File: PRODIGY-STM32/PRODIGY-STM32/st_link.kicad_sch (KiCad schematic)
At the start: 27 parts, among them Q1 BC850, U1 STM32F103C8Tx, Y1 8MHz

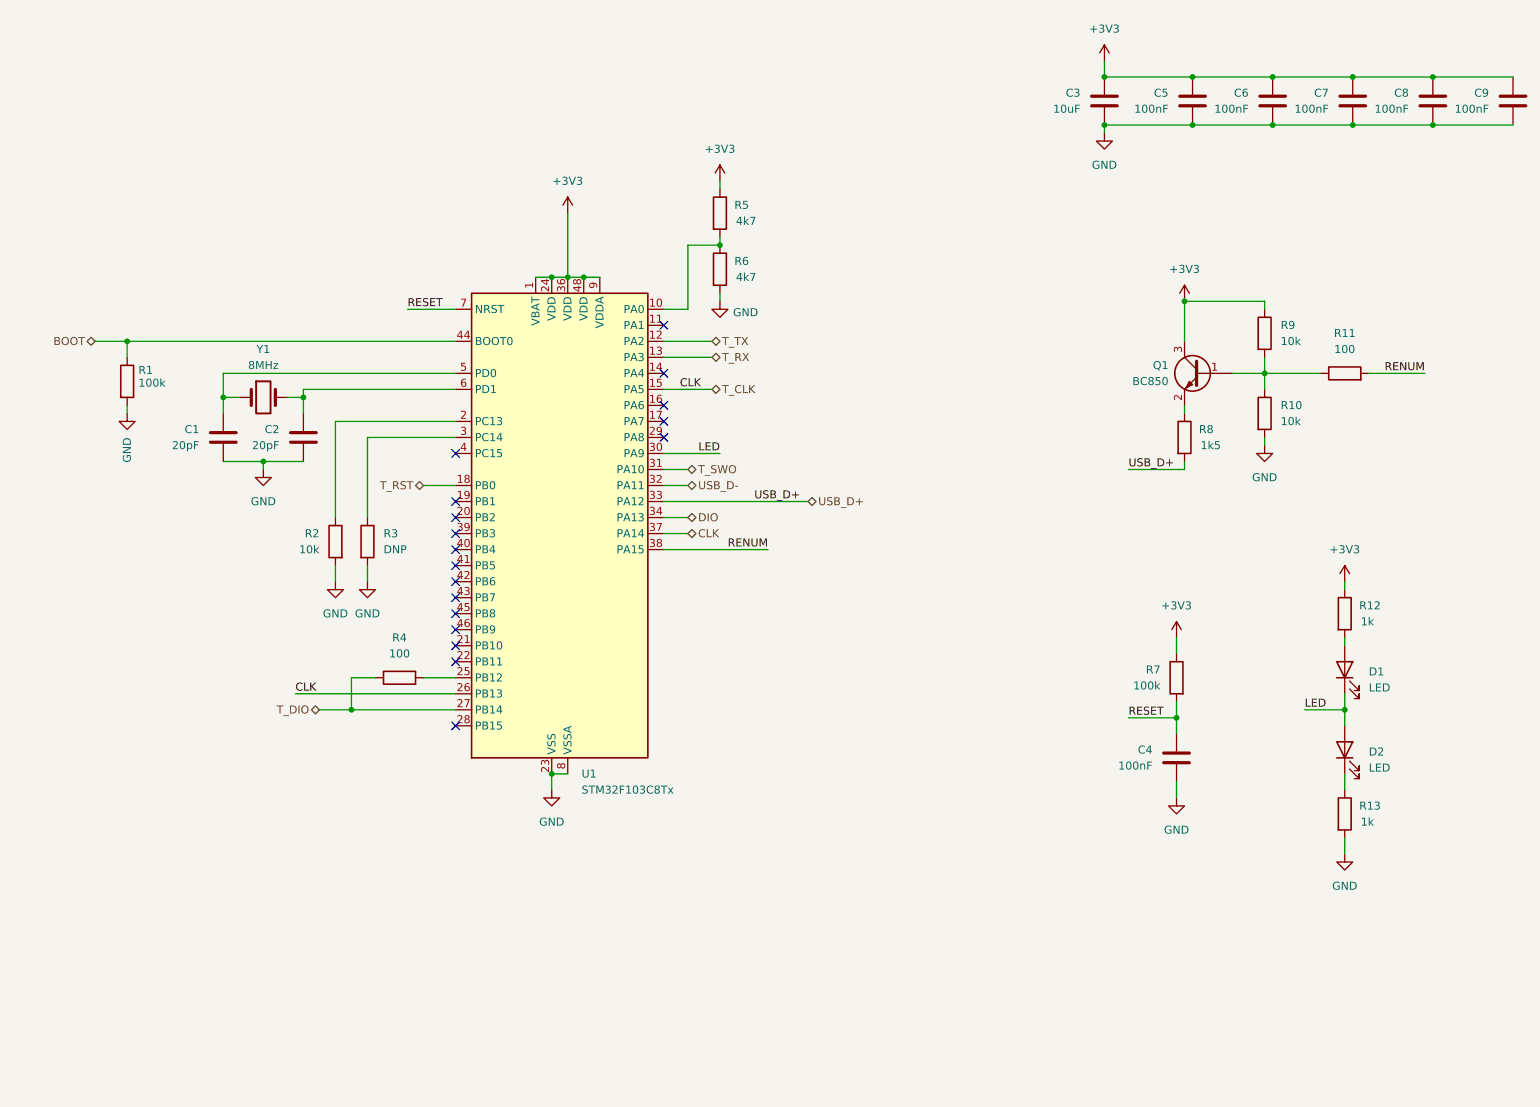
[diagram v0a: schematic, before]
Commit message: stm32 schematic finished
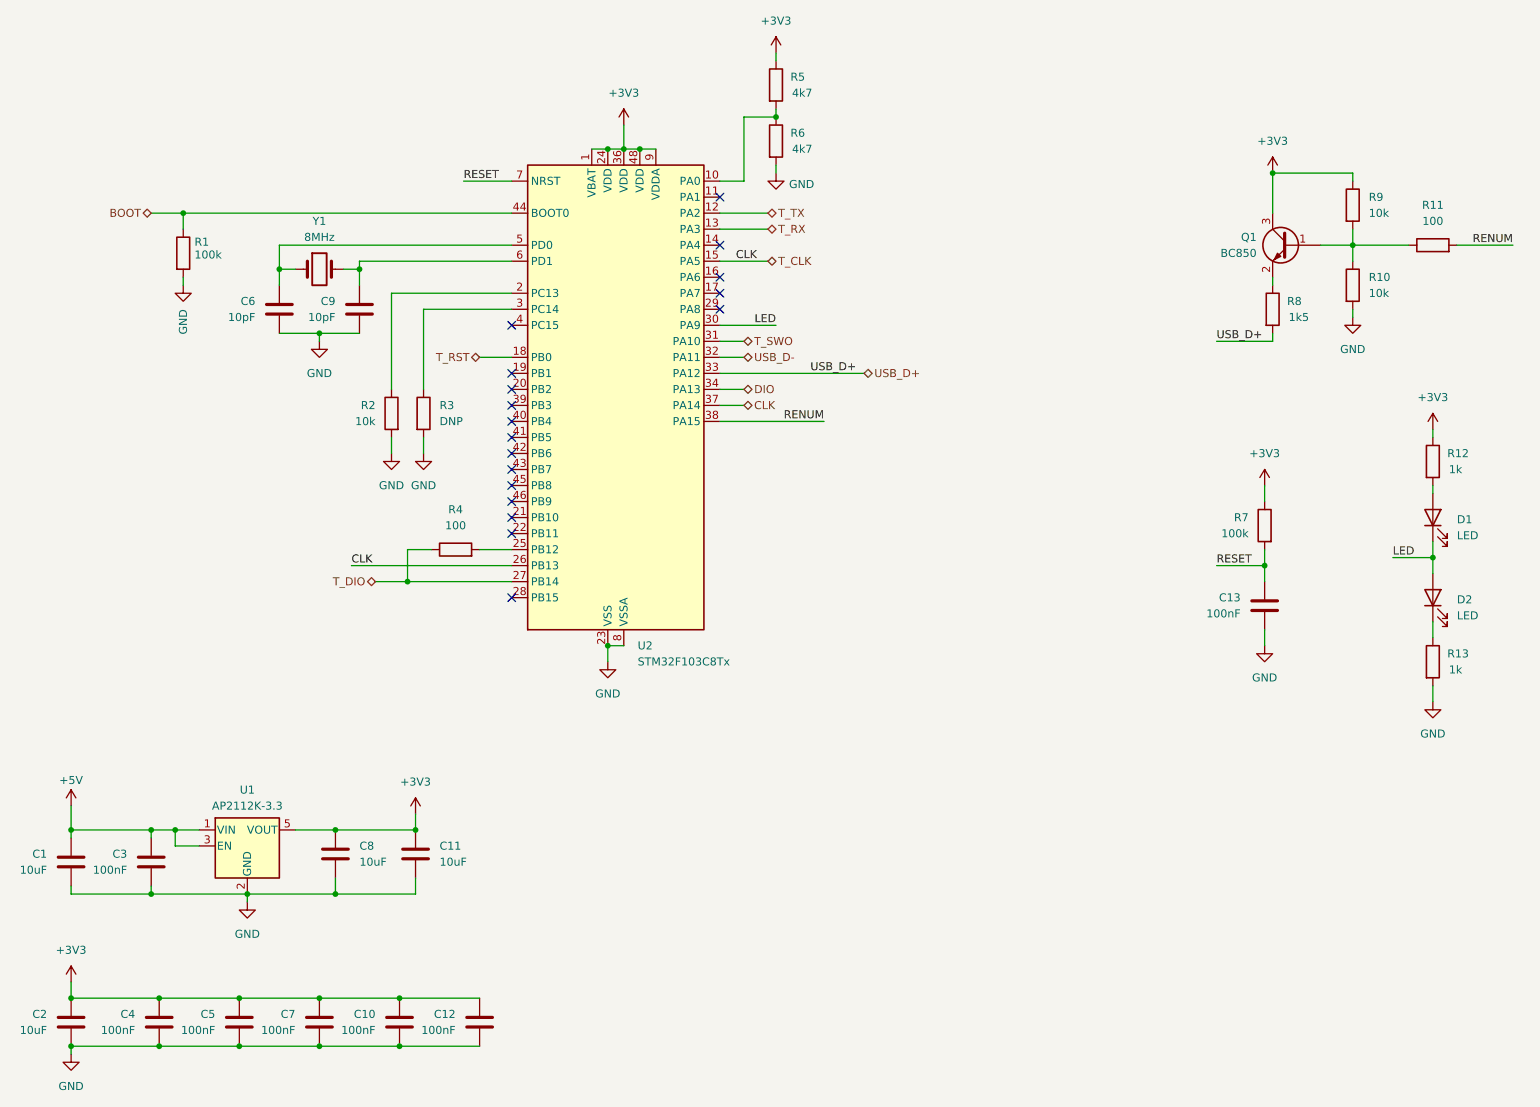
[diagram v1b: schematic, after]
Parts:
- added C1, C11, C8: 10uF, symbol Device:C
- added C3: 100nF, symbol Device:C
- added U1: AP2112K-3.3, Package_TO_SOT_SMD:SOT-23-5, symbol Regulator_Linear:AP2112K-3.3
- C6: renamed from C1; value 20pF -> 10pF
- C9: renamed from C2; value 20pF -> 10pF
- renumbered C8 to C10, C9 to C12, C4 to C13, C3 to C2, C5 to C4, C6 to C5, U1 to U2
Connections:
- net +3V3: now also C11.1, C8.1, U1.5 (VOUT)
- net GND: now also C1.2, C11.2, C3.2, C8.2, U1.2 (GND)
- new net +5V: C1.1, C3.1, U1.1 (VIN), U1.3 (EN)
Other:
- moved on the sheet: C10, C12, C13, C2, C4, C5, C6, C7, C9, D1, D2, Q1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

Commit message: All footprint assosiations have been made across all schematics.
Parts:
- C1, C11, C2, C8: footprint (none) -> Capacitor_SMD:C_0805_2012Metric
- C10, C12, C13, C3, C4, C5, C6, C7, C9: footprint (none) -> Capacitor_SMD:C_0603_1608Metric
- D1, D2: footprint (none) -> LED_SMD:LED_0805_2012Metric
- R1, R10, R11, R12, R13, R2, R3, R4, R5, R6, R7, R8, R9: footprint (none) -> Resistor_SMD:R_0603_1608Metric
- Y1: footprint (none) -> Crystal:Crystal_SMD_3225-4Pin_3.2x2.5mm
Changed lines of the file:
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@@
 			)
 		)
-		(property "Footprint" ""
+		(property "Footprint" "Capacitor_SMD:C_0603_1608Metric"
 			(at 222.5548 119.38 0)
 			(effects
@@
 			)
 		)
-		(property "Footprint" ""
+		(property "Footprint" "Resistor_SMD:R_0603_1608Metric"
 			(at 86.868 85.09 90)
 			(effects
@@
 			)
 		)
-		(property "Footprint" ""
+		(property "Footprint" "Resistor_SMD:R_0603_1608Metric"
 			(at 144.272 33.02 90)
 			(effects
@@
 			)
 		)
-		(property "Footprint" ""
+		(property "Footprint" "Capacitor_SMD:C_0603_1608Metric"
 			(at 98.0948 185.42 0)
 			(effects
@@
 			)
 		)
-		(property "Footprint" ""
+		(property "Footprint" "Capacitor_SMD:C_0603_1608Metric"
 			(at 85.3948 185.42 0)
 			(effects
@@
 			)
 		)
-		(property "Footprint" ""
+		(property "Footprint" "Capacitor_SMD:C_0805_2012Metric"
 			(at 33.3248 160.02 0)
 			(effects
@@
 			)
 		)
-		(property "Footprint" ""
+		(property "Footprint" "Capacitor_SMD:C_0603_1608Metric"
 			(at 59.9948 185.42 0)
 			(effects
@@
 			)
 		)
-		(property "Footprint" ""
+		(property "Footprint" "Resistor_SMD:R_0603_1608Metric"
 			(at 50.292 59.69 90)
 			(effects
@@
 			)
 		)
-		(property "Footprint" ""
+		(property "Footprint" "Capacitor_SMD:C_0603_1608Metric"
 			(at 72.6948 185.42 0)
 			(effects
@@
 			)
 		)
-		(property "Footprint" ""
+		(property "Footprint" "Resistor_SMD:R_0603_1608Metric"
 			(at 235.712 52.07 90)
 			(effects
@@
 			)
 		)
-		(property "Footprint" ""
+		(property "Footprint" "Capacitor_SMD:C_0603_1608Metric"
 			(at 79.0448 72.39 0)
 			(effects
@@
 			)
 		)
-		(property "Footprint" ""
+		(property "Footprint" "Capacitor_SMD:C_0603_1608Metric"
 			(at 47.2948 185.42 0)
 			(effects
@@
 			)
 		)
-		(property "Footprint" ""
+		(property "Footprint" "Resistor_SMD:R_0603_1608Metric"
 			(at 88.392 85.09 90)
 			(effects
@@
 			)
 		)
-		(property "Footprint" ""
+		(property "Footprint" "Capacitor_SMD:C_0603_1608Metric"
 			(at 66.3448 72.39 0)
 			(effects
@@
 			)
 		)
-		(property "Footprint" ""
+		(property "Footprint" "Resistor_SMD:R_0603_1608Metric"
 			(at 95.25 108.458 90)
 			(effects
@@
 			)
 		)
-		(property "Footprint" ""
+		(property "Footprint" "Resistor_SMD:R_0603_1608Metric"
 			(at 248.412 124.46 90)
 			(effects
@@
 			)
 		)
-		(property "Footprint" ""
+		(property "Footprint" "LED_SMD:LED_0805_2012Metric"
 			(at 250.19 114.3 0)
 			(effects
@@
 			)
 		)
-		(property "Footprint" ""
+		(property "Footprint" "Capacitor_SMD:C_0805_2012Metric"
 			(at 77.1652 158.75 0)
 			(effects
@@
 			)
 		)
-		(property "Footprint" ""
+		(property "Footprint" "Resistor_SMD:R_0603_1608Metric"
 			(at 250.19 60.198 90)
 			(effects
@@
 			)
 		)
-		(property "Footprint" ""
+		(property "Footprint" "Capacitor_SMD:C_0805_2012Metric"
 			(at 89.8652 158.75 0)
 			(effects
@@
 			)
 		)
-		(property "Footprint" ""
+		(property "Footprint" "Resistor_SMD:R_0603_1608Metric"
 			(at 235.712 64.77 90)
 			(effects
@@
 			)
 		)
-		(property "Footprint" ""
+		(property "Footprint" "Resistor_SMD:R_0603_1608Metric"
 			(at 225.298 102.87 90)
 			(effects
@@
 			)
 		)
-		(property "Footprint" ""
+		(property "Footprint" "LED_SMD:LED_0805_2012Metric"
 			(at 250.19 101.6 0)
 			(effects
@@
 			)
 		)
-		(property "Footprint" ""
+		(property "Footprint" "Resistor_SMD:R_0603_1608Metric"
 			(at 248.412 92.71 90)
 			(effects
@@
 			)
 		)
-		(property "Footprint" ""
+		(property "Footprint" "Resistor_SMD:R_0603_1608Metric"
 			(at 223.012 68.58 90)
 			(effects
@@
 			)
 		)
-		(property "Footprint" ""
+		(property "Footprint" "Resistor_SMD:R_0603_1608Metric"
 			(at 144.272 41.91 90)
 			(effects
@@
 			)
 		)
-		(property "Footprint" ""
+		(property "Footprint" "Crystal:Crystal_SMD_3225-4Pin_3.2x2.5mm"
 			(at 73.66 62.23 0)
 			(effects
@@
 			)
 		)
-		(property "Footprint" ""
+		(property "Footprint" "Capacitor_SMD:C_0805_2012Metric"
 			(at 33.3248 185.42 0)
 			(effects
@@
 			)
 		)
-		(property "Footprint" ""
+		(property "Footprint" "Capacitor_SMD:C_0603_1608Metric"
 			(at 46.0248 160.02 0)
 			(effects

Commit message: STM32 bom done.
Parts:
- C1, C11, C2, C8: TME (none) -> CL21A106KOQNNNE
- C10, C12, C13, C3, C4, C5, C7: TME (none) -> CL10B104KB8NNNC
- C6, C9: TME (none) -> 0603N100J500CT
- D1: TME (none) -> OF-SMD2012R
- D2: TME (none) -> OF-SMD2012B
- Q1: TME (none) -> BC850B-DIO
- R1, R7: TME (none) -> CRCW0603100KJNTABC
- R10, R2, R9: TME (none) -> WR06X1002FTL
- R11, R4: TME (none) -> SMD0603-100R
- R12, R13: TME (none) -> RC0603JR-071K
- R3: TME (none) -> SMD0603-0R; now not fitted
- R5, R6: TME (none) -> CRCW06034K70FKTABC
- R8: TME (none) -> WR06X1501FTL
- U1: TME (none) -> AP2112K-3.3TRG1
- U2: TME (none) -> STM32F103C8T6
- Y1: footprint Crystal:Crystal_SMD_3225-4Pin_3.2x2.5mm -> Crystal:Crystal_SMD_5032-4Pin_5.0x3.2mm; TME (none) -> 8.00M-CFPX104

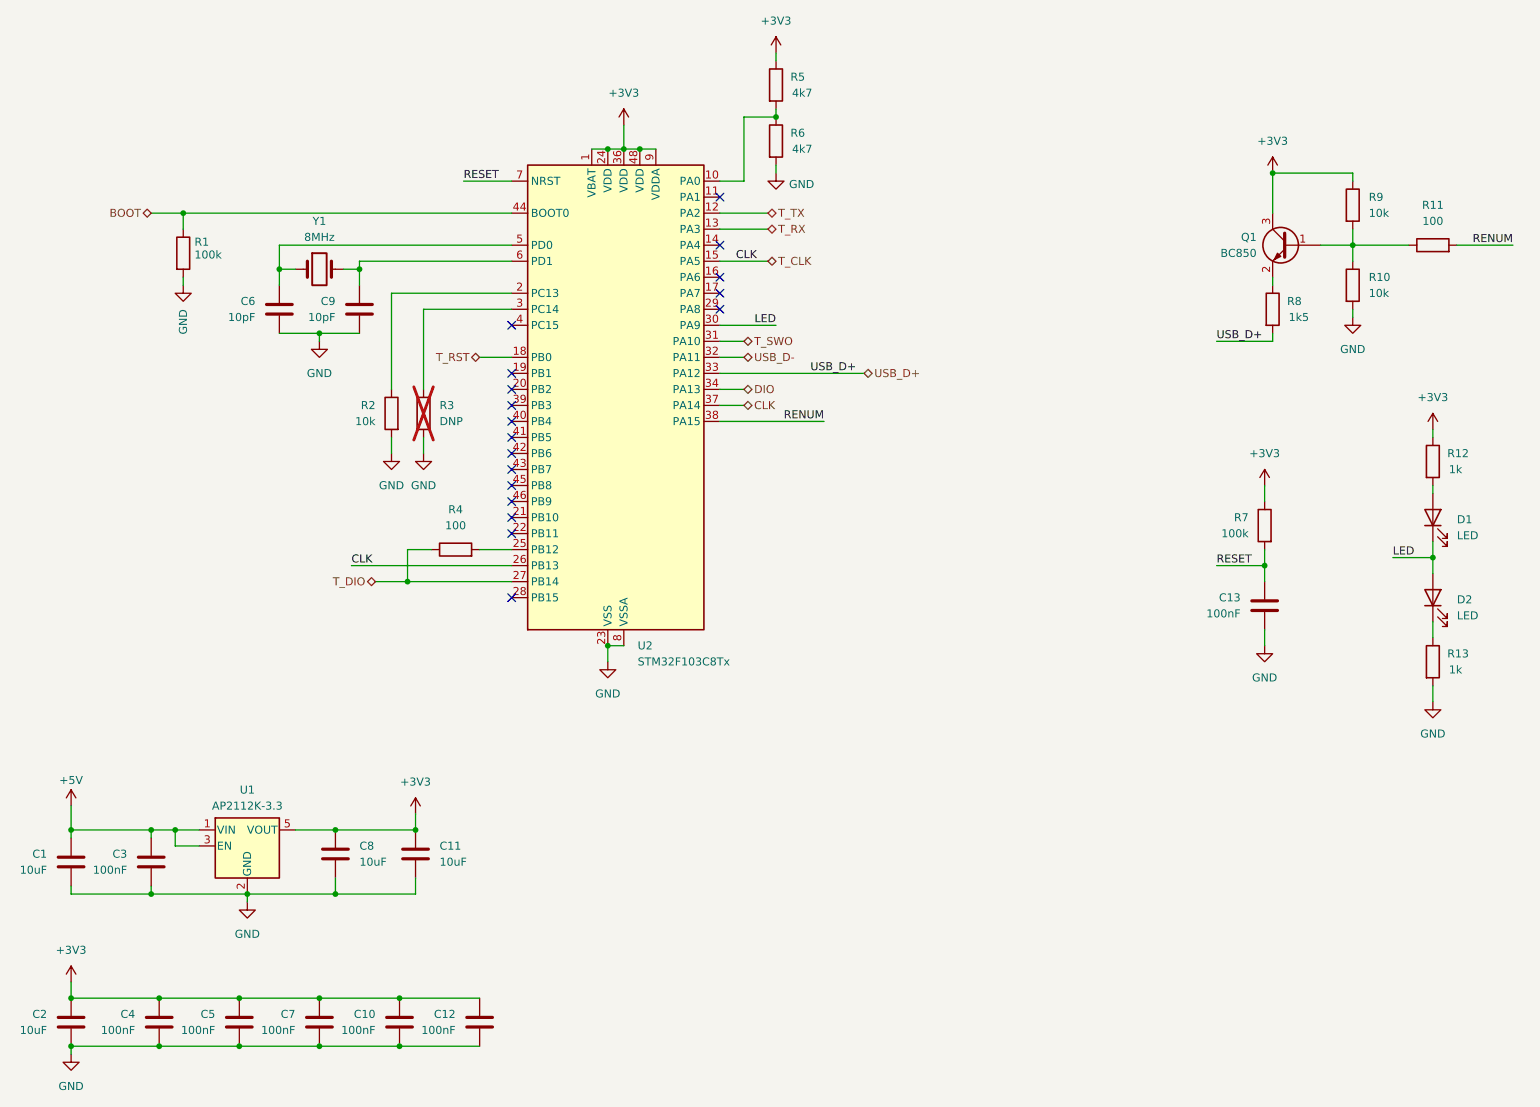
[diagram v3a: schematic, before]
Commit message: stm32 started, footprints updated, lazout started
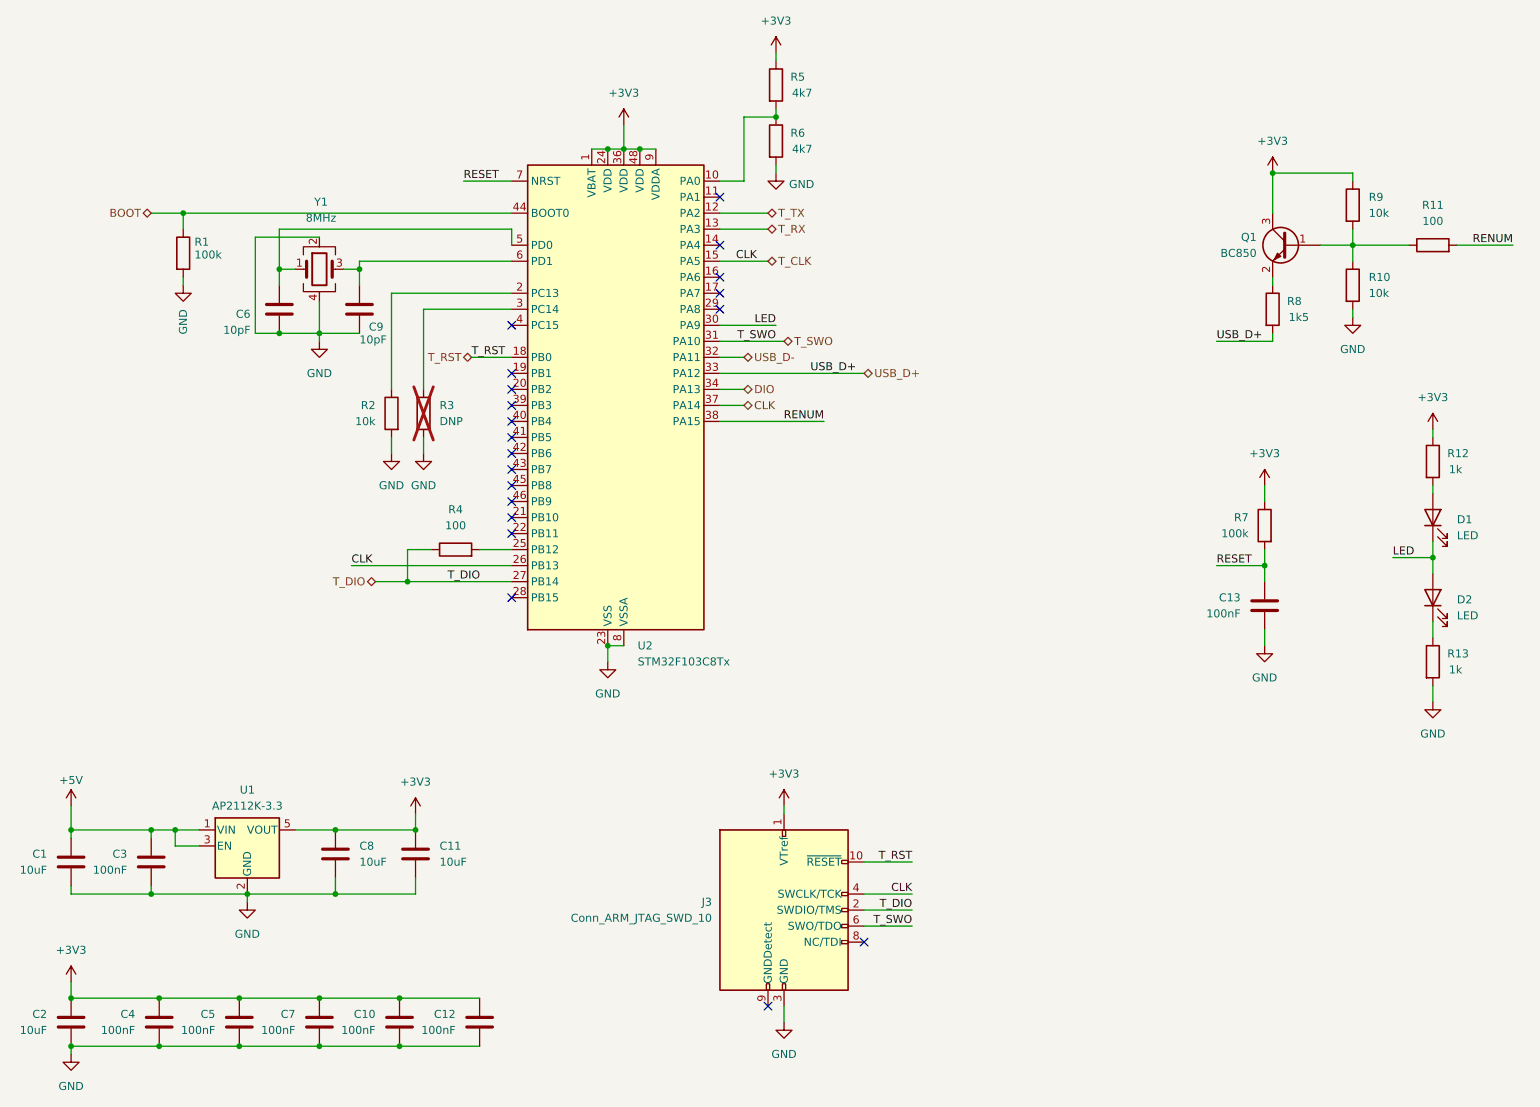
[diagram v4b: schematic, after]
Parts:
- removed Y1: 8MHz, Crystal:Crystal_SMD_5032-4Pin_5.0x3.2mm, symbol Device:Crystal
- added J3: Conn_ARM_JTAG_SWD_10, Connector_IDC:IDC-Header_2x05_P2.54mm_Vertical, symbol Connector:Conn_ARM_JTAG_SWD_10
- added Y1: 8MHz, Crystal:Crystal_SMD_5032-4Pin_5.0x3.2mm, symbol Device:Crystal_GND24
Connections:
- net +3V3: now also J3.1 (VTref)
- net CLK: now also J3.4 (SWCLK/TCK)
- net GND: now also J3.3 (GND), J3.5 (GND), Y1.2, Y1.4
- net T_DIO: now also J3.2 (SWDIO/TMS)
- net T_RST: now also J3.10 (~{RESET})
- net T_SWO: now also J3.6 (SWO/TDO)
- net at C9.1, U2.6 (PD1): now also Y1.3
- net at C6.1, U2.5 (PD0): now also Y1.1
- no-connect marks 18 -> 20
